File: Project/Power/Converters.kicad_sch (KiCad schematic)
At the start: 7 parts, among them U17 AP63203WU

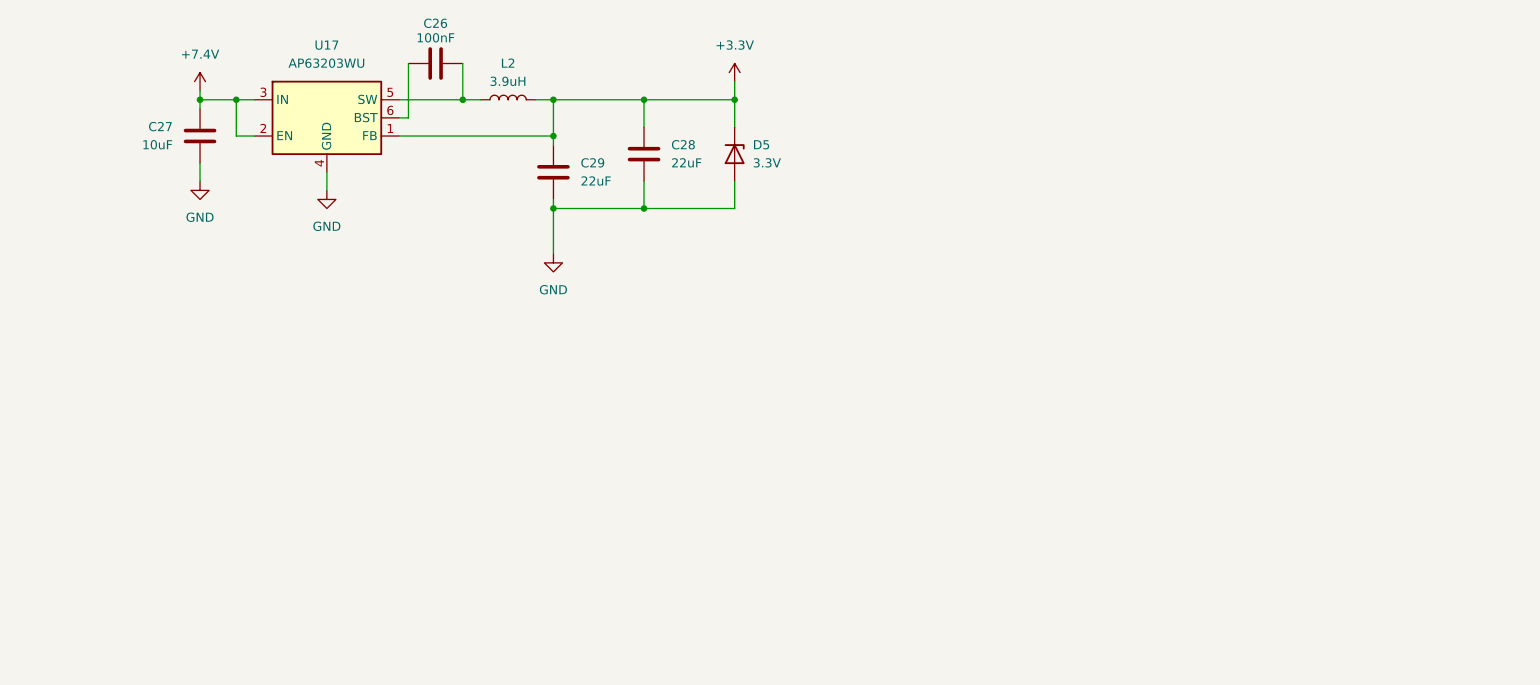
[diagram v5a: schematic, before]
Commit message: Reorganize converters
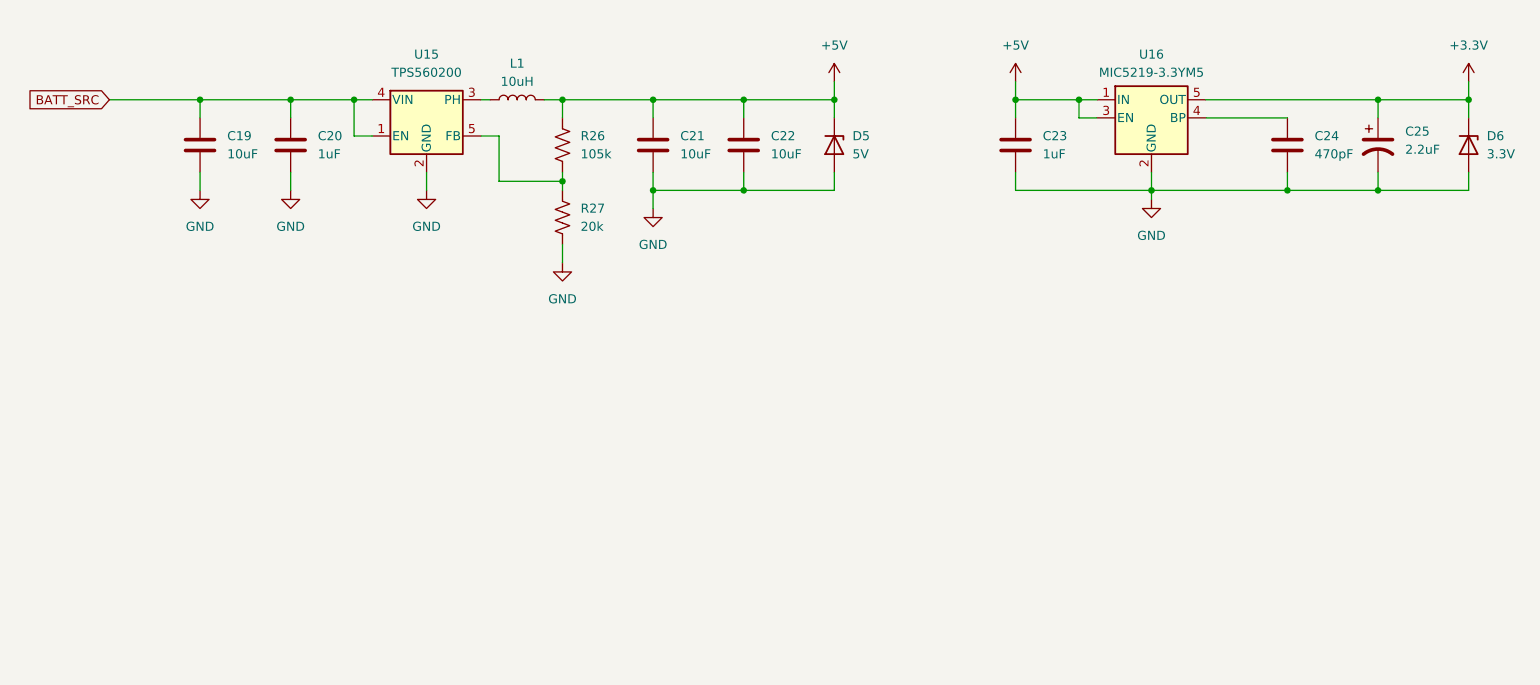
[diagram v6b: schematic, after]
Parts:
- removed C26: 100nF, Capacitor_SMD:C_0402_1005Metric, symbol Device:C
- removed C27: 10uF, Capacitor_SMD:C_1206_3216Metric, symbol Device:C
- removed C28, C29: 22uF, Capacitor_SMD:C_0603_1608Metric, symbol Device:C
- removed L2: 3.9uH, Inductor_SMD:L_Pulse_PA4334, symbol Device:L
- removed U17: AP63203WU, Package_TO_SOT_SMD:TSOT-23-6, symbol Regulator_Switching:AP63203WU
- added C19, C21, C22: 10uF, Capacitor_SMD:C_1206_3216Metric, symbol Device:C
- added C20, C23: 1uF, Capacitor_SMD:C_0603_1608Metric, symbol Device:C
- added C24: 470pF, Capacitor_SMD:C_0603_1608Metric, symbol Device:C
- added C25: 2.2uF, Capacitor_Tantalum_SMD:CP_EIA-3216-18_Kemet-A, symbol Device:C_Polarized_US
- added D6: 3.3V, Diode_SMD:D_MicroSMP_KA, symbol Device:D_Zener
- added L1: 10uH, Inductor_SMD:L_1210_3225Metric, symbol Device:L
- added R26: 105k, Resistor_SMD:R_0603_1608Metric, symbol Device:R_US
- added R27: 20k, Resistor_SMD:R_0603_1608Metric, symbol Device:R_US
- added U15: TPS560200, Package_TO_SOT_SMD:SOT-23-5, symbol Regulator_Switching:TPS560200
- added U16: MIC5219-3.3YM5, Package_TO_SOT_SMD:SOT-23-5, symbol Regulator_Linear:MIC5219-3.3YM5
- D5: value 3.3V -> 5V; Listing https://www.digikey.com/en/products/detail/vishay-general-semiconductor-diodes-division/MSP3V3-M3-89A/2071748 -> https://www.digikey.com/en/products/detail/vishay-general-semiconductor-diodes-division/MSP5-0A-M3-89A/2071749
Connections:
- net +3.3V: now also C25.1, D6.1 (K), U16.5 (OUT); no longer D5.1 (K)
- net GND: now also C19.2, C20.2, C21.2, C22.2, C23.2, C24.2, C25.2, D6.2 (A), R27.2, U15.2 (GND), U16.2 (GND)
- new net: R26.2, R27.1, U15.5 (FB)
- new net: C24.1, U16.4 (BP)
- new net: L1.1, U15.3 (PH)
- new net +5V: C21.1, C22.1, C23.1, D5.1 (K), L1.2, R26.1, U16.1 (IN), U16.3 (EN)
- new net BATT_SRC: C19.1, C20.1, U15.1 (EN), U15.4 (VIN)
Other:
- moved on the sheet: D5

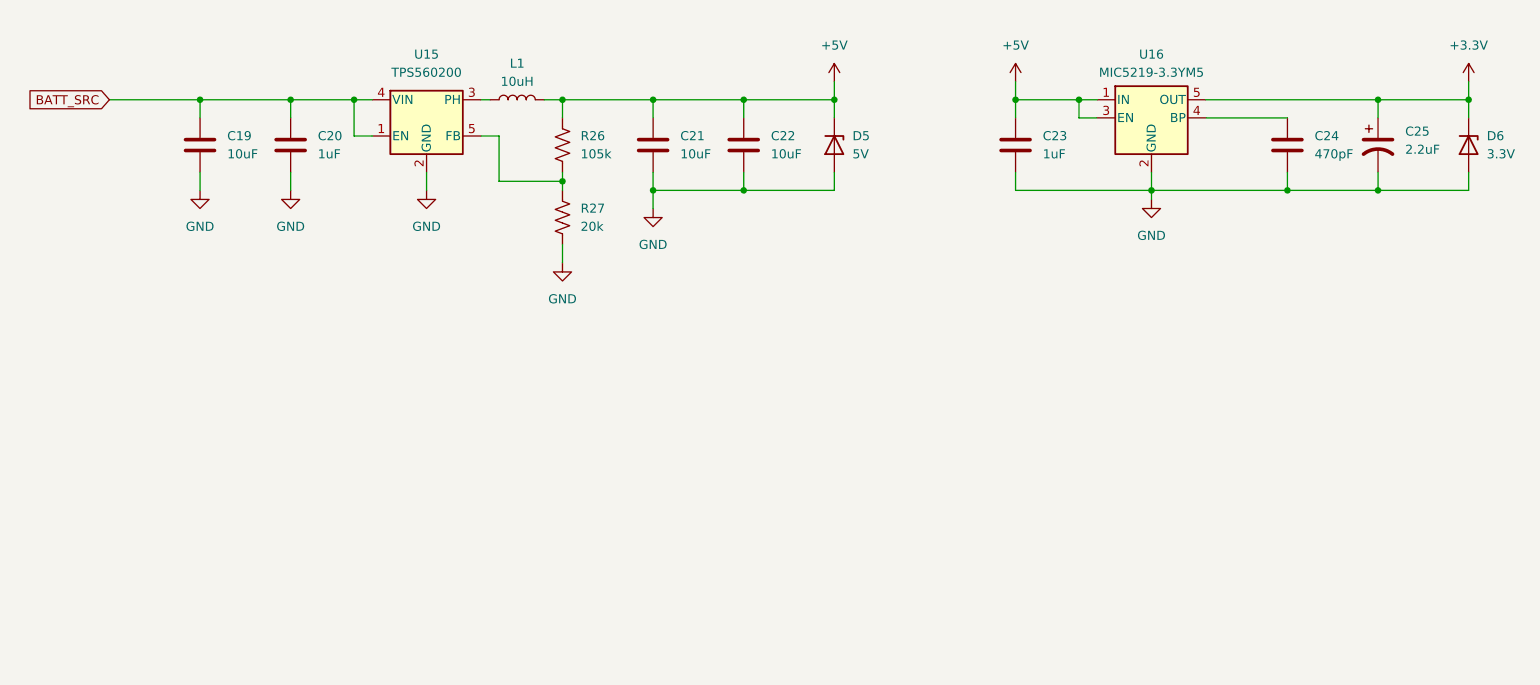
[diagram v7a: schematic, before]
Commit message: Add 5V 2A voltage regulator
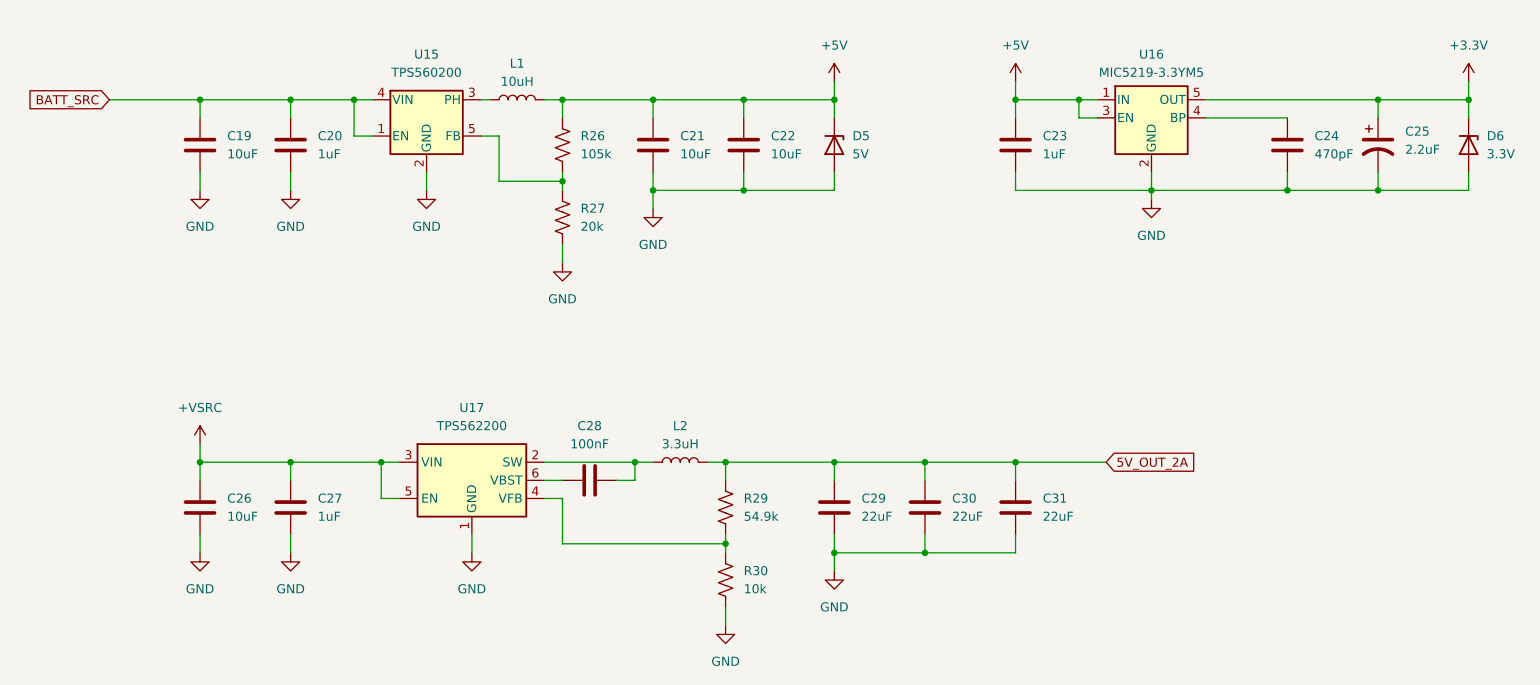
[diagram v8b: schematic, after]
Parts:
- added C26: 10uF, Capacitor_SMD:C_1206_3216Metric, symbol Device:C
- added C27: 1uF, Capacitor_SMD:C_0603_1608Metric, symbol Device:C
- added C28: 100nF, Capacitor_SMD:C_0603_1608Metric, symbol Device:C
- added C29, C30, C31: 22uF, Capacitor_SMD:C_1206_3216Metric, symbol Device:C
- added L2: 3.3uH, Inductor_SMD:L_Pulse_PA4340, symbol Device:L
- added R29: 54.9k, Resistor_SMD:R_0603_1608Metric, symbol Device:R_US
- added R30: 10k, Resistor_SMD:R_0603_1608Metric, symbol Device:R_US
- added U17: TPS562200, Package_TO_SOT_SMD:SOT-23-6, symbol Regulator_Switching:TPS562200
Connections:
- net GND: now also C26.2, C27.2, C29.2, C30.2, C31.2, R30.1, U17.1 (GND)
- new net: R29.2, R30.2, U17.4 (VFB)
- new net: C28.2, L2.1, U17.2 (SW)
- new net: C28.1, U17.6 (VBST)
- new net +VSRC: C26.1, C27.1, U17.3 (VIN), U17.5 (EN)
- new net 5V_OUT_2A: C29.1, C30.1, C31.1, L2.2, R29.1
